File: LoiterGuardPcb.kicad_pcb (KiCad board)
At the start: 4 copper layers, 90 x 80 mm, 198 parts, among them IC1 SI4435DYPBF, IC2 SI4435DYPBF, IC3 KTA1170GVAE-TB, J1 B3B-XH-A, J10 878980204, J11 B16B-PH-SM4-TB_LF__SN_, J12 532610971, J2 ARJM11D7-114-AB-EW2, J3 B6B-PH-SM4-TB, J4 B2B-PH-K-S, J5 5033981892, J6 B2B-PH-K-S, J7 B6B-PH-SM4-TB, J8 B2B-PH-K-S, J9 B2B-PH-K-S, Q1 MBT3904DW1, Q2 BSS138, Q3 PDTC114EU_115, Q4 PDTC114EU_115, Q5 PDTC114EU_115, Q6 AO3400A, Q7 AO3400A, U1 TPS2378DDAR(HSOIC-8), U10 NL-SW-LTE-TC4NAG-B, U11 74AHC1G08, U12 MCP23017_ML, U13 DFR0299, U2 LMR33630ADDAR, U3 TX4138(ESOIC-8), U4 TX4138(ESOIC-8), U5 AP62201Z6-7, U6 AP62201Z6-7, U7 W5500, U8 ESP32-S3-WROOM-1-N16R8, U9 TPL5010

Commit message: layout checkin
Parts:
- removed C57: 0.1uF, Capacitor_SMD:C_0603_1608Metric
- moved R60 71.0 mm to (99.5, 98.9), turned to -90 degrees
- moved R58 70.7 mm to (99.9, 95.8), turned to -90 degrees
- moved U11 67.6 mm to (102.5, 95.4), turned to 90 degrees
- moved JP1 67.4 mm to (102.1, 99.1), turned to 180 degrees
- moved TP8 59.0 mm to (138.8, 101.8)
- moved Q2 43.0 mm to (185.5, 92.9)
- moved J4 38.5 mm to (182.6, 98.5)
- moved R47 38.5 mm to (182.4, 103.7)
- moved R48 38.5 mm to (183.9, 103.8)
- moved R50 7.12 mm to (136.2, 90.5), turned to 90 degrees
- moved R49 7.03 mm to (137.3, 90.4), turned to 90 degrees
- moved TP4 6.93 mm to (121.3, 101.0)
- moved R44 2.92 mm to (132.4, 80.0), turned to 0 degrees
- moved R45 2.46 mm to (134.1, 74.9)
- moved Q1 2.46 mm to (132.3, 77.5)
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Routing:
- net /MCU/MM_TX: track 0.00 -> 98.9 mm, vias 0 -> 4
- net /MCU/MM_RX: track 0.00 -> 97.6 mm, vias 0 -> 4
- net /Expander/~{SD_CS}: track 0.00 -> 87.4 mm, vias 0 -> 5
- net +3V3: track 18.0 -> 102.9 mm, vias 24 -> 19
- net /Expander/CAM_SD_MOSI: track 0.00 -> 82.7 mm, vias 0 -> 5
- net /MCU/LED3: track 0.00 -> 75.7 mm, vias 0 -> 3
- net /MCU/LED: track 0.00 -> 75.2 mm, vias 0 -> 4
- net /Expander/CAM_SD_SCLK: track 0.00 -> 73.8 mm, vias 0 -> 3
- net /MCU/LED2: track 0.00 -> 71.3 mm, vias 0 -> 3
- net /Expander/CAM_SD_MISO: track 0.00 -> 68.8 mm, vias 0 -> 2
- net /MCU/STROBE/USB+: track 0.00 -> 67.5 mm, vias 0 -> 3
- net /Expander/~{MM_RST}: track 0.00 -> 67.3 mm, vias 0 -> 3
- net /MCU/MM_RTS: track 0.00 -> 66.5 mm, vias 0 -> 3
- net GND: track 38.6 -> 104.9 mm, vias 20 -> 25
- net /MCU/CELL_CTS: track 0.00 -> 65.2 mm, vias 0 -> 2
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- added copper zone on In4.Cu, net +12VDC
- added copper zone on In4.Cu, net +12VP
- added copper zone on In4.Cu, net +3V3
- added copper zone on In4.Cu, net +5V
- added copper zone on In4.Cu, net +5VDC
- added copper zone on In4.Cu, net /Poe/POE+
- added copper zone on In4.Cu, net /Poe/POE-
- removed copper zone on In2.Cu, net +12VDC
- removed copper zone on In2.Cu, net +12VP
- removed copper zone on In2.Cu, net +3V3
- removed copper zone on In2.Cu, net +5V
- removed copper zone on In2.Cu, net +5VDC
- removed copper zone on In2.Cu, net /Poe/POE+
- removed copper zone on In2.Cu, net /Poe/POE-
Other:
- copper layers 4 -> 6

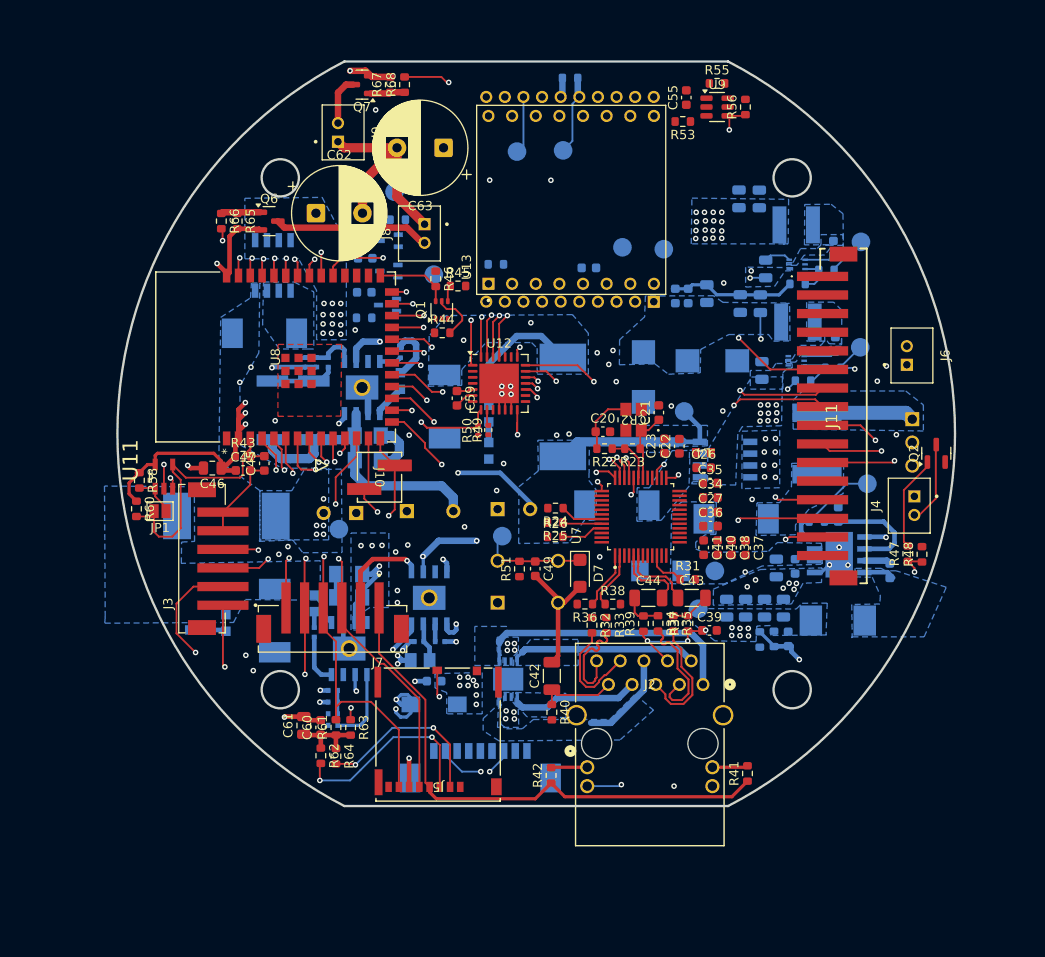
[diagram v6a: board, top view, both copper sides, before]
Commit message: WIP - starting moving reference silkscreens around
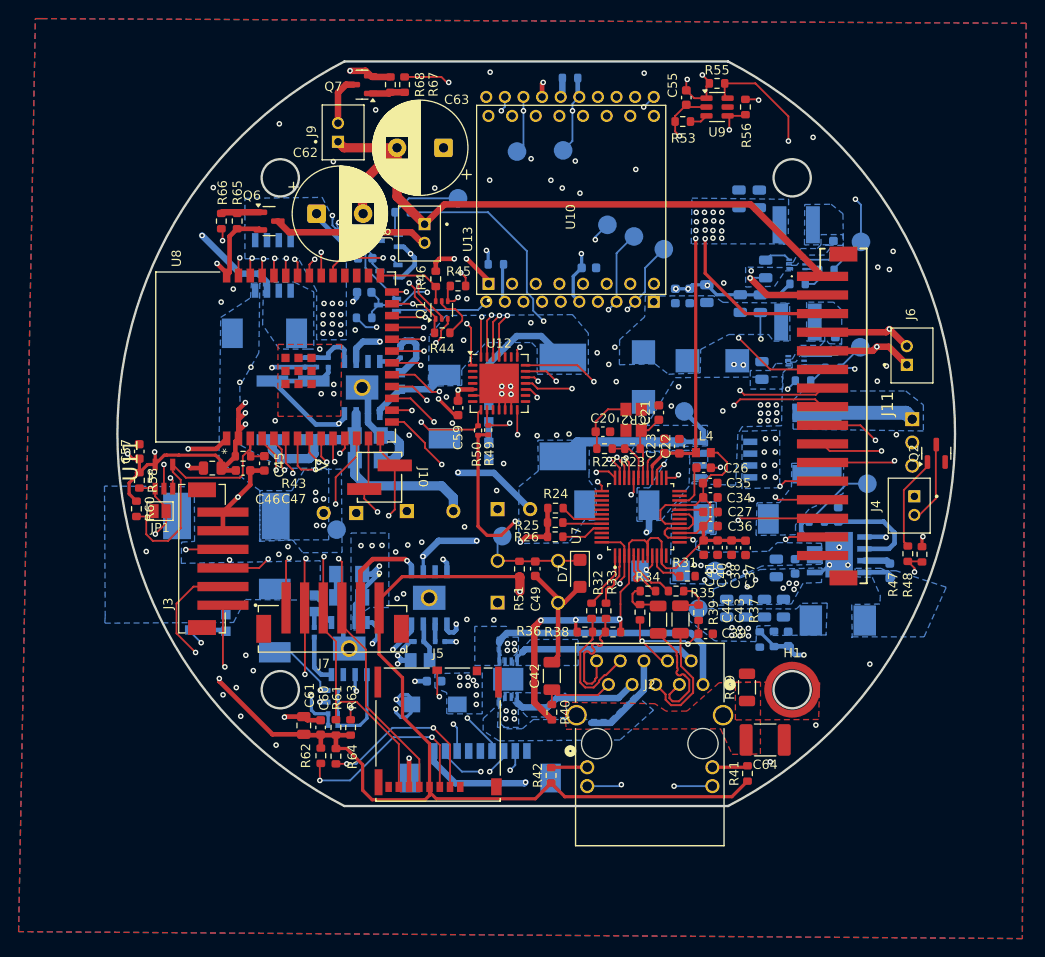
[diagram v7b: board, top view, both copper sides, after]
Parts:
- added C57: 0.1uF, Capacitor_SMD:C_0603_1608Metric, F.Cu at (99.8, 92.7)
- added C64: 2.2nF, Capacitor_SMD:C_1812_4532Metric, F.Cu at (167.1, 123.7)
- added H1: MountingHole_Pad, MountingHole:MountingHole_3mm_Pad_TopOnly, F.Cu at (170.0, 118.3)
- added R69: 1M, Resistor_SMD:R_1206_3216Metric, F.Cu at (165.2, 118.0)
- moved TP14 19.4 mm to (150.2, 68.3)
- moved TP9 6.86 mm to (134.1, 65.5)
- moved R34 3.64 mm to (154.5, 107.7), turned to 180 degrees
- moved R35 3.49 mm to (157.5, 107.7), turned to 0 degrees
- moved R38 3.00 mm to (150.8, 112.1)
- moved R36 3.00 mm to (147.7, 112.1)
- moved C43 2.61 mm to (158.0, 110.8), turned to -90 degrees
- moved C44 2.56 mm to (155.6, 110.8), turned to -90 degrees
- moved TP11 1.70 mm to (153.0, 69.6)
- moved R37 1.62 mm to (159.9, 110.0)
- moved R32 1.55 mm to (148.4, 109.8)
- moved R33 1.55 mm to (150.0, 109.8)
- moved R39 1.28 mm to (153.7, 110.0)
- moved C59 1.05 mm to (134.1, 88.0)
- moved R52 0.96 mm to (128.2, 67.0)
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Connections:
- C43 pad 1: /Poe/RX_P -> /Poe/RX2_P
- C43 pad 2: /Poe/RX_P -> /Poe/RX3_P
- C44 pad 1: /Poe/RX_N -> /Poe/RX2_N
- C44 pad 2: /Poe/RX_N -> /Poe/RX3_N
- J2 pad 10: /Poe/TX_P -> /Poe/TX2_P
- J2 pad 15: (no net) -> GNDPWR
- J2 pad 16: (no net) -> GNDPWR
- J2 pad 3: /Poe/RX_N -> /Poe/RX3_N
- J2 pad 5: /Poe/RX_P -> /Poe/RX3_P
- J2 pad 8: /Poe/TX_N -> /Poe/TX2_N
- R32 pad 1: /Poe/TX_N -> /Poe/TX1_N
- R32 pad 2: /Poe/TX_N -> /Poe/TX2_N
- R33 pad 1: /Poe/TX_P -> /Poe/TX1_P
- R33 pad 2: /Poe/TX_P -> /Poe/TX2_P
- R34 pad 1: /Poe/RX_N -> /Poe/RX1_N
- R34 pad 2: /Poe/RX_N -> /Poe/RX2_N
- R35 pad 1: /Poe/RX_P -> /Poe/RX1_P
- R35 pad 2: /Poe/RX_P -> /Poe/RX2_P
- R36 pad 1: /Poe/TX_N -> /Poe/TX2_N
- R37 pad 2: /Poe/RX_P -> /Poe/RX2_P
- R38 pad 1: /Poe/TX_P -> /Poe/TX2_P
- R39 pad 2: /Poe/RX_N -> /Poe/RX2_N
- U7 pad 1: /Poe/TX_N -> /Poe/TX1_N
- U7 pad 2: /Poe/TX_P -> /Poe/TX1_P
- U7 pad 5: /Poe/RX_N -> /Poe/RX1_N
- U7 pad 6: /Poe/RX_P -> /Poe/RX1_P
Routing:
- net +3V3: track 102.9 -> 312.7 mm, vias 19 -> 32
- net +5V: track 1.69 -> 113.9 mm, vias 11 -> 15
- net /MCU/~{WD_RESET}: track 2.60 -> 111.7 mm, vias 1 -> 4
- net GND: track 104.9 -> 190.2 mm, vias 25 -> 61
- net +12V: track 24.6 -> 101.6 mm, vias 0 -> 1
- net +3.3VA: track 0.00 -> 75.7 mm, vias 0 -> 3
- net /MCU/MM_TX: track 98.9 -> 164.8 mm, vias 4 -> 6
- net /MCU/MM_RX: track 97.6 -> 162.1 mm, vias 4 -> 6
- net /MCU/~{DTR}: track 5.26 -> 64.7 mm, vias 1 -> 4
- net /MCU/MM_CTS: track 7.99 -> 66.6 mm, vias 1 -> 2
- net /MCU/~{PROG_RST}: track 4.63 -> 62.1 mm, vias 0 -> 3
- net /MCU/~{RTS}: track 5.59 -> 62.7 mm, vias 1 -> 3
- net Net-(U10-ON_OFF): track 0.00 -> 53.1 mm, vias 0 -> 4
- net /Outputs/SPK1: track 0.00 -> 48.9 mm, vias 0 -> 2
- net /Expander/CELL_ON_OFF: track 1.53 -> 48.2 mm, vias 1 -> 3
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- added copper zone on F.Cu, net GNDPWR

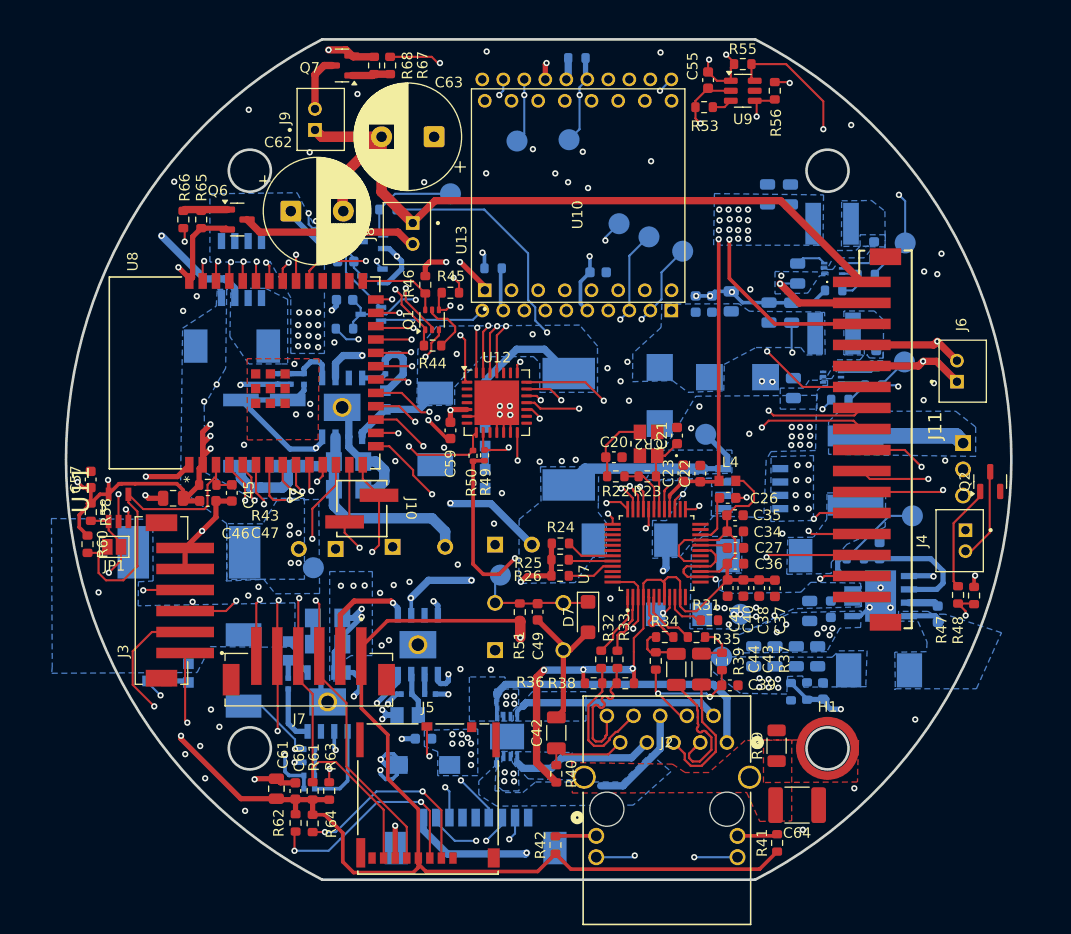
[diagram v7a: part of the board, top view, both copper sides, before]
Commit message: moved 12V connector to the front layer
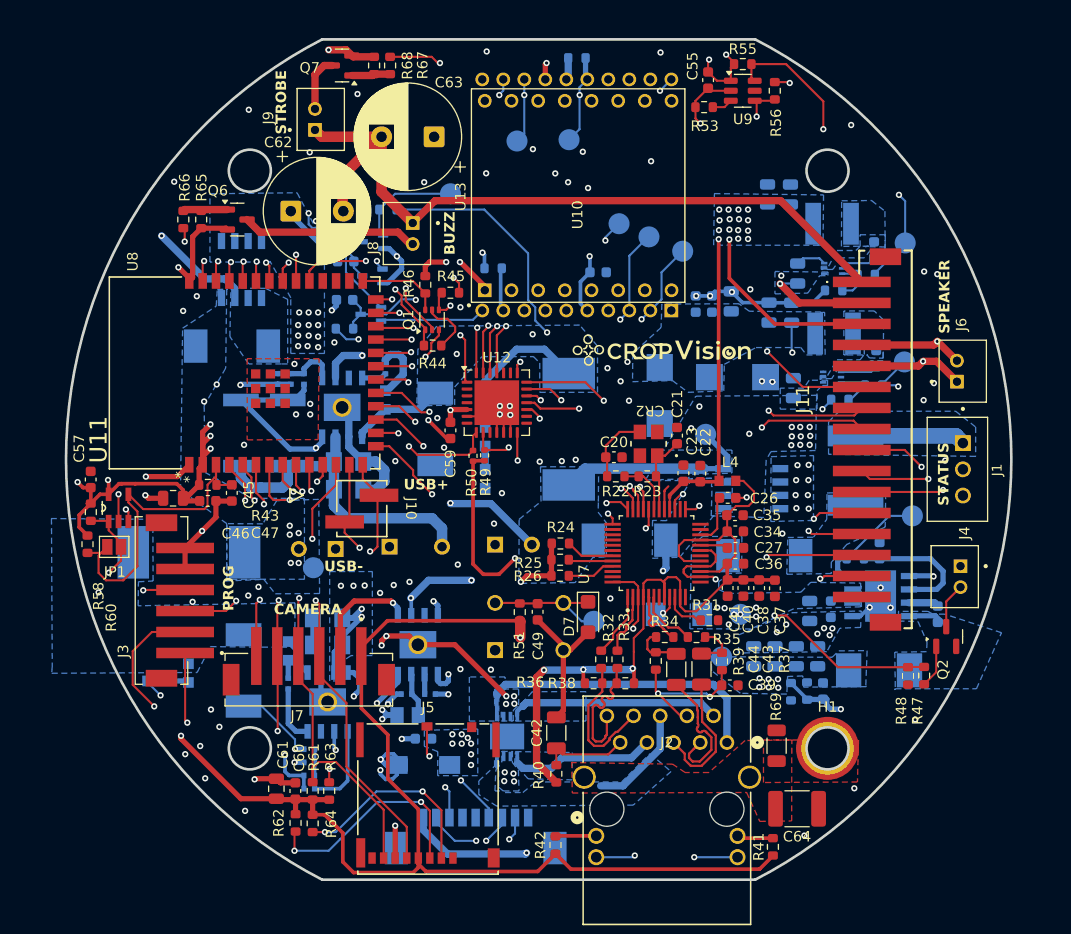
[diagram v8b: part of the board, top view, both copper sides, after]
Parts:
- J1: moved to F.Cu
- moved Q2 15.3 mm to (181.3, 107.7)
- moved TP8 9.93 mm to (147.8, 106.2)
- moved R48 9.90 mm to (177.7, 111.4), turned to -90 degrees
- moved R47 8.33 mm to (179.2, 111.4), turned to -90 degrees
- moved J4 3.46 mm to (182.1, 102.0)
- moved J1 1.07 mm to (182.4, 91.7)
- moved R41 0.55 mm to (164.8, 127.7)
- moved C64 0.35 mm to (167.1, 124.0)
- moved C5 0.30 mm to (130.8, 99.1)
- moved R7 0.07 mm to (122.4, 108.5)
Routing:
- net /Poe/POE-: track 17.6 -> 32.5 mm
- net Net-(Q2-G): track 10.2 -> 4.08 mm
- net /MCU/LED: track 75.2 -> 70.3 mm, vias 4 -> 3
- net Net-(Q2-D): track 8.25 -> 4.33 mm
- net GND: track 190.2 -> 189.1 mm, vias 61 -> 59
- net +5V: track 113.9 -> 114.9 mm
- net /MCU/SETUP: track 49.7 -> 50.5 mm
- net +3V3: track 312.7 -> 312.2 mm
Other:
- board text added: "BUZZ"
- board text added: "CAMERA"
- board text added: "PROG"
- board text added: "SPEAKER"
- board text added: "STATUS"
- board text added: "STROBE"
- board text added: "USB+"
- board text added: "USB-"
- board text added: "~{RTS}"
